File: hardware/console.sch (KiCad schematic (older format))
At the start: 26 parts, among them J4 IGC, J5 Micro USB, J6 BT_KEY, J7 UART, U2 MAX3232, U3 CH340G, Y1 12M

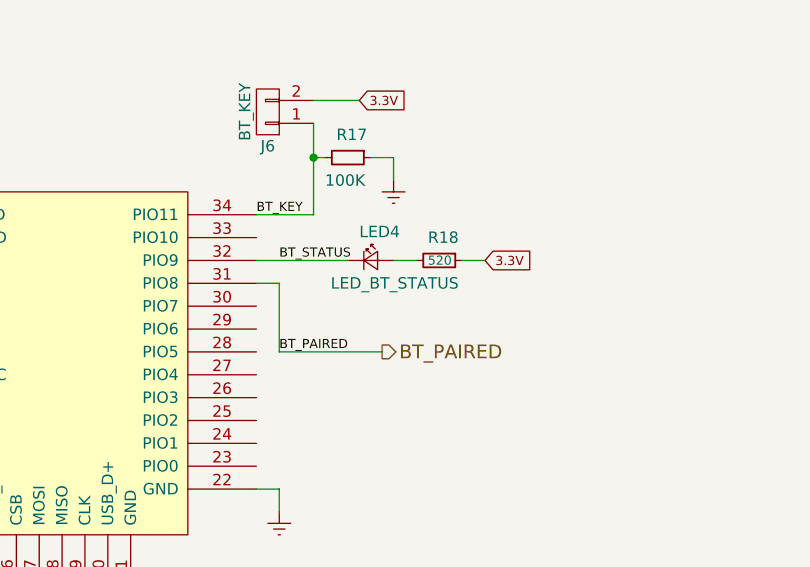
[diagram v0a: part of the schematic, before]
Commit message: Prepare fabrication layer for assembly
* Proper placement of labels on F.Fab layer
* Element outlines
* Correct values of used components
* LED values indicate color, rather then function
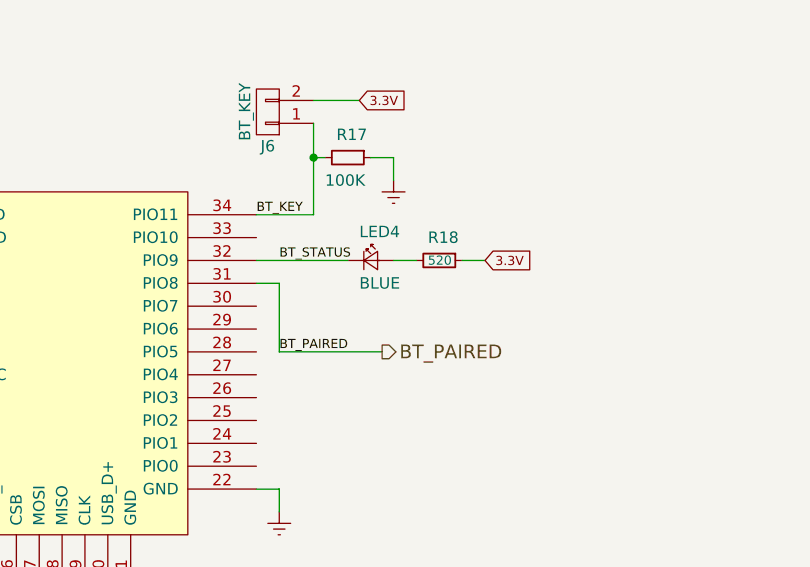
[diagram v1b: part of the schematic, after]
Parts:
- LED4: value LED_BT_STATUS -> BLUE
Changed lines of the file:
@@
 P 5750 5850
 F 0 "LED4" H 5700 5975 50  0000 L CNN
-F 1 "LED_BT_STATUS" H 5575 5750 50  0000 L CNN
+F 1 "BLUE" H 5700 5750 50  0000 L CNN
 F 2 "LEDs:LED_0603" V 5750 5850 50  0001 C CNN
 F 3 "" V 5750 5850 50  0001 C CNN

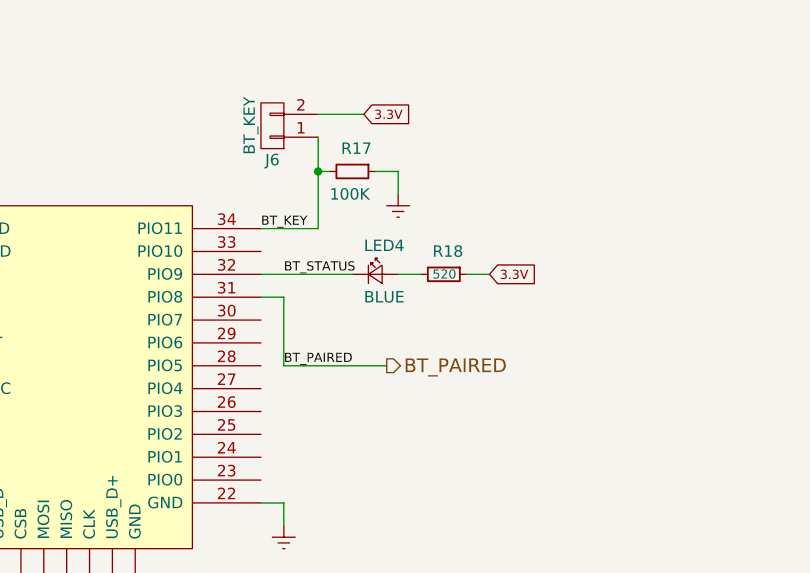
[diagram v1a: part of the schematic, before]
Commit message: Changes and fixes for 0.7
* Different 4-pin reset button (because I have a lot of those)
* Bluethooth "paired" and "status" leds swapped - dashboard
  led will show "paired" status and will not annoyingly blink all
  the time
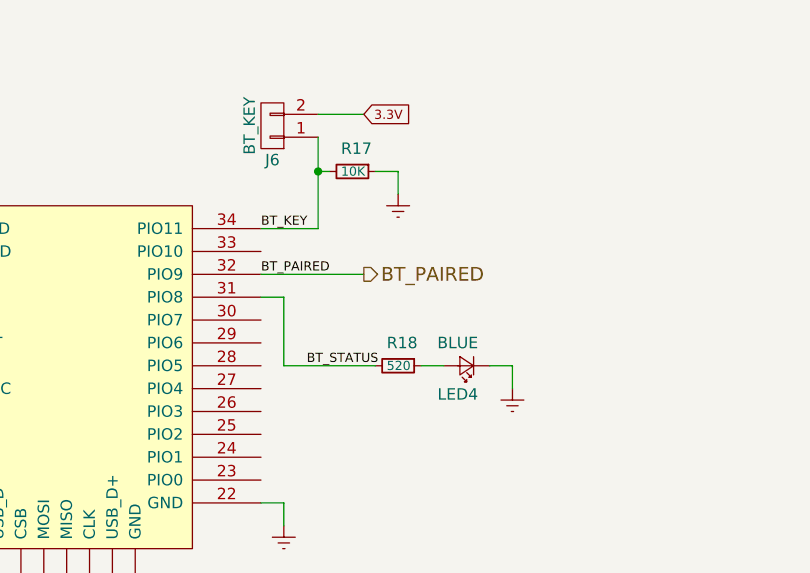
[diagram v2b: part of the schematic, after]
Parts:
- R17: value 100K -> 10K
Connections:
- wire segments 115 -> 116
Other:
- moved on the sheet: LED4, R18
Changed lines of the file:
@@
 Text Label 1450 2850 0    40   ~ 0
 CON_RX
-Text HLabel 5800 6250 2    60   Output ~ 0
+Text HLabel 5700 5850 2    60   Output ~ 0
 BT_PAIRED
 Text Label 8100 2250 0    40   ~ 0
@@
 P 5650 5400
 F 0 "R17" V 5550 5350 50  0000 L CNN
-F 1 "100K" V 5750 5300 50  0000 L CNN
+F 1 "10K" V 5650 5350 40  0000 L CNN
 F 2 "Resistors_SMD:R_0805" H 5650 5400 50  0001 C CNN
 F 3 "" H 5650 5400 50  0001 C CNN
@@
 L LED_Small LED4
 U 1 1 5A2F840B
-P 5750 5850
-F 0 "LED4" H 5700 5975 50  0000 L CNN
-F 1 "BLUE" H 5700 5750 50  0000 L CNN
-F 2 "LEDs:LED_0603" V 5750 5850 50  0001 C CNN
-F 3 "" V 5750 5850 50  0001 C CNN
-	1    5750 5850
-	1    0    0    -1
+P 6150 6250
+F 0 "LED4" H 6100 6375 50  0000 L CNN
+F 1 "BLUE" H 6100 6150 50  0000 L CNN
+F 2 "LEDs:LED_0603" V 6150 6250 50  0001 C CNN
+F 3 "" V 6150 6250 50  0001 C CNN
+	1    6150 6250
+	-1   0    0    1
 $EndComp
 $Comp
 L R_Small R18
 U 1 1 5A2F84BF
-P 6050 5850
-F 0 "R18" V 5950 5800 50  0000 L CNN
-F 1 "520" V 6050 5800 40  0000 L CNN
-F 2 "Resistors_SMD:R_0805" H 6050 5850 50  0001 C CNN
-F 3 "" H 6050 5850 50  0001 C CNN
-	1    6050 5850
+P 5850 6250
+F 0 "R18" V 5750 6200 50  0000 L CNN
+F 1 "520" V 5850 6200 40  0000 L CNN
+F 2 "Resistors_SMD:R_0805" H 5850 6250 50  0001 C CNN
+F 3 "" H 5850 6250 50  0001 C CNN
+	1    5850 6250
 	0    1    1    0
 $EndComp
 Wire Wire Line
-	5250 5850 5650 5850
-Wire Wire Line
-	5850 5850 5950 5850
-Wire Wire Line
-	6150 5850 6250 5850
-Text GLabel 6250 5850 2    40   Input ~ 0
-3.3V
-Text Label 5350 5850 0    40   ~ 0
+	5350 6250 5750 6250
+Wire Wire Line
+	5950 6250 6050 6250
+Wire Wire Line
+	6250 6250 6350 6250
+Text Label 5450 6250 0    40   ~ 0
 BT_STATUS
 Wire Wire Line
@@
 	5350 5950 5350 6250
 Wire Wire Line
-	5350 6250 5800 6250
-Text Label 5350 6250 0    40   ~ 0
+	5250 5850 5700 5850
+Text Label 5250 5850 0    40   ~ 0
 BT_PAIRED
 Wire Wire Line
@@
 Wire Wire Line
 	9150 3100 9400 3100
+$Comp
+L Earth #PWR?
+U 1 1 5A7708E8
+P 6350 6350
+F 0 "#PWR?" H 6350 6100 50  0001 C CNN
+F 1 "Earth" H 6350 6200 50  0001 C CNN
+F 2 "" H 6350 6350 50  0001 C CNN
+F 3 "" H 6350 6350 50  0001 C CNN
+	1    6350 6350
+	1    0    0    -1
+$EndComp
+Wire Wire Line
+	6350 6250 6350 6350
 $EndSCHEMATC

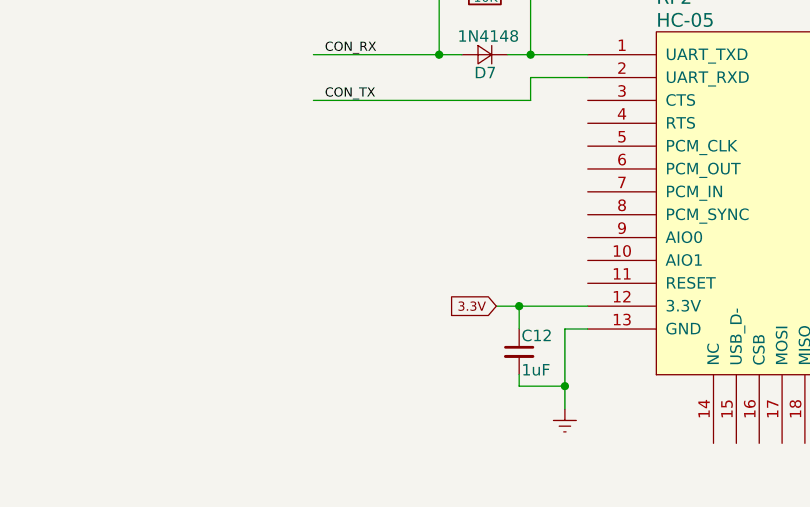
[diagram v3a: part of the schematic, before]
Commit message: Reset button resets bluetooth chip as well
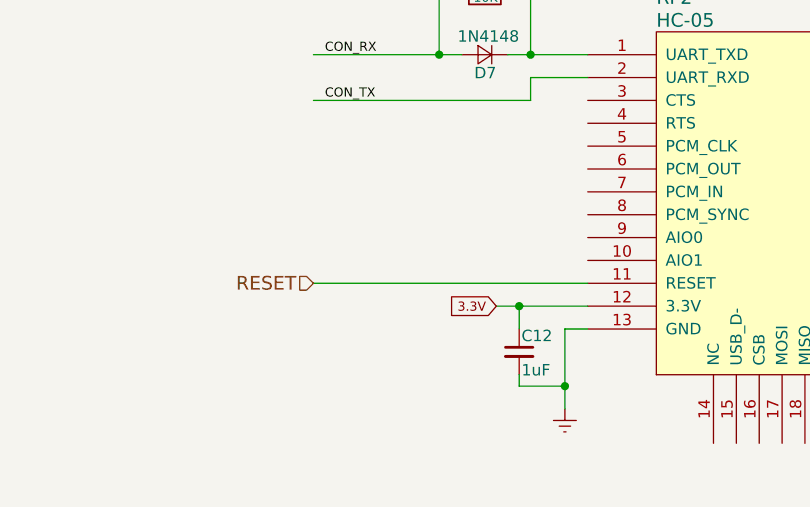
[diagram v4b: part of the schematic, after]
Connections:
- net labels added: RESET
- wire segments 116 -> 117
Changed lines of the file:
@@
 Wire Wire Line
 	6350 6250 6350 6350
+Wire Wire Line
+	3450 6650 2250 6650
+Text HLabel 2250 6650 0    60   Input ~ 0
+RESET
 $EndSCHEMATC

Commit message: Correct capacitor size
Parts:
- C27: footprint Capacitors_SMD:C_1206 -> Capacitors_SMD:C_0805
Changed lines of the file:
@@
 F 0 "C27" H 8060 1420 50  0000 L CNN
 F 1 "100nF" H 8060 1270 50  0000 L CNN
-F 2 "Capacitors_SMD:C_1206" H 8050 1350 50  0001 C CNN
+F 2 "Capacitors_SMD:C_0805" H 8050 1350 50  0001 C CNN
 F 3 "" H 8050 1350 50  0001 C CNN
 	1    8050 1350
